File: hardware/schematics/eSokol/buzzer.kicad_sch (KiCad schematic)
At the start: 6 parts, among them Q3 BC547

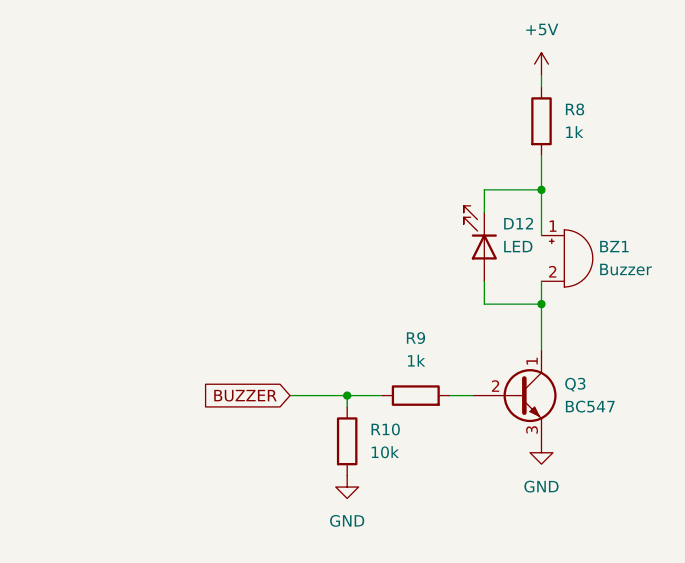
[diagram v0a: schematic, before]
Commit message: hardware/schematics: Replace screen-based control for HC-05 smartphone-app-based control, add buzzer RC filter, rework cold LED circuit
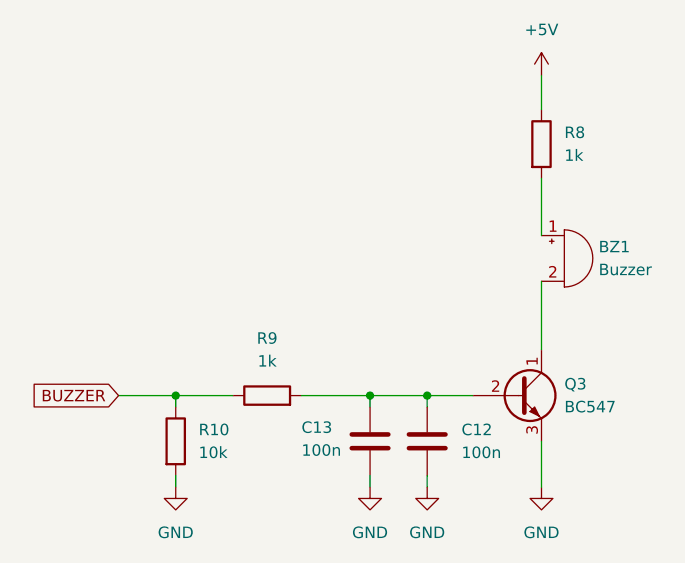
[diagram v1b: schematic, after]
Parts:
- removed D12: LED, symbol Device:LED
- added C12, C13: 100n, symbol Device:C
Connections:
- net GND: now also C12.2, C13.2
- net at Q3.2 (B), R9.2: now also C12.1, C13.1
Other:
- moved on the sheet: R10, R8, R9

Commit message: WIP: update some schematics to reflect the newest design changes
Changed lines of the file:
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@@
 (kicad_sch
-	(version 20231120)
+	(version 20250114)
 	(generator "eeschema")
-	(generator_version "8.0")
+	(generator_version "9.0")
 	(paper "A4")
 	(junction
